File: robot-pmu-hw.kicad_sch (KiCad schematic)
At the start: 0 parts

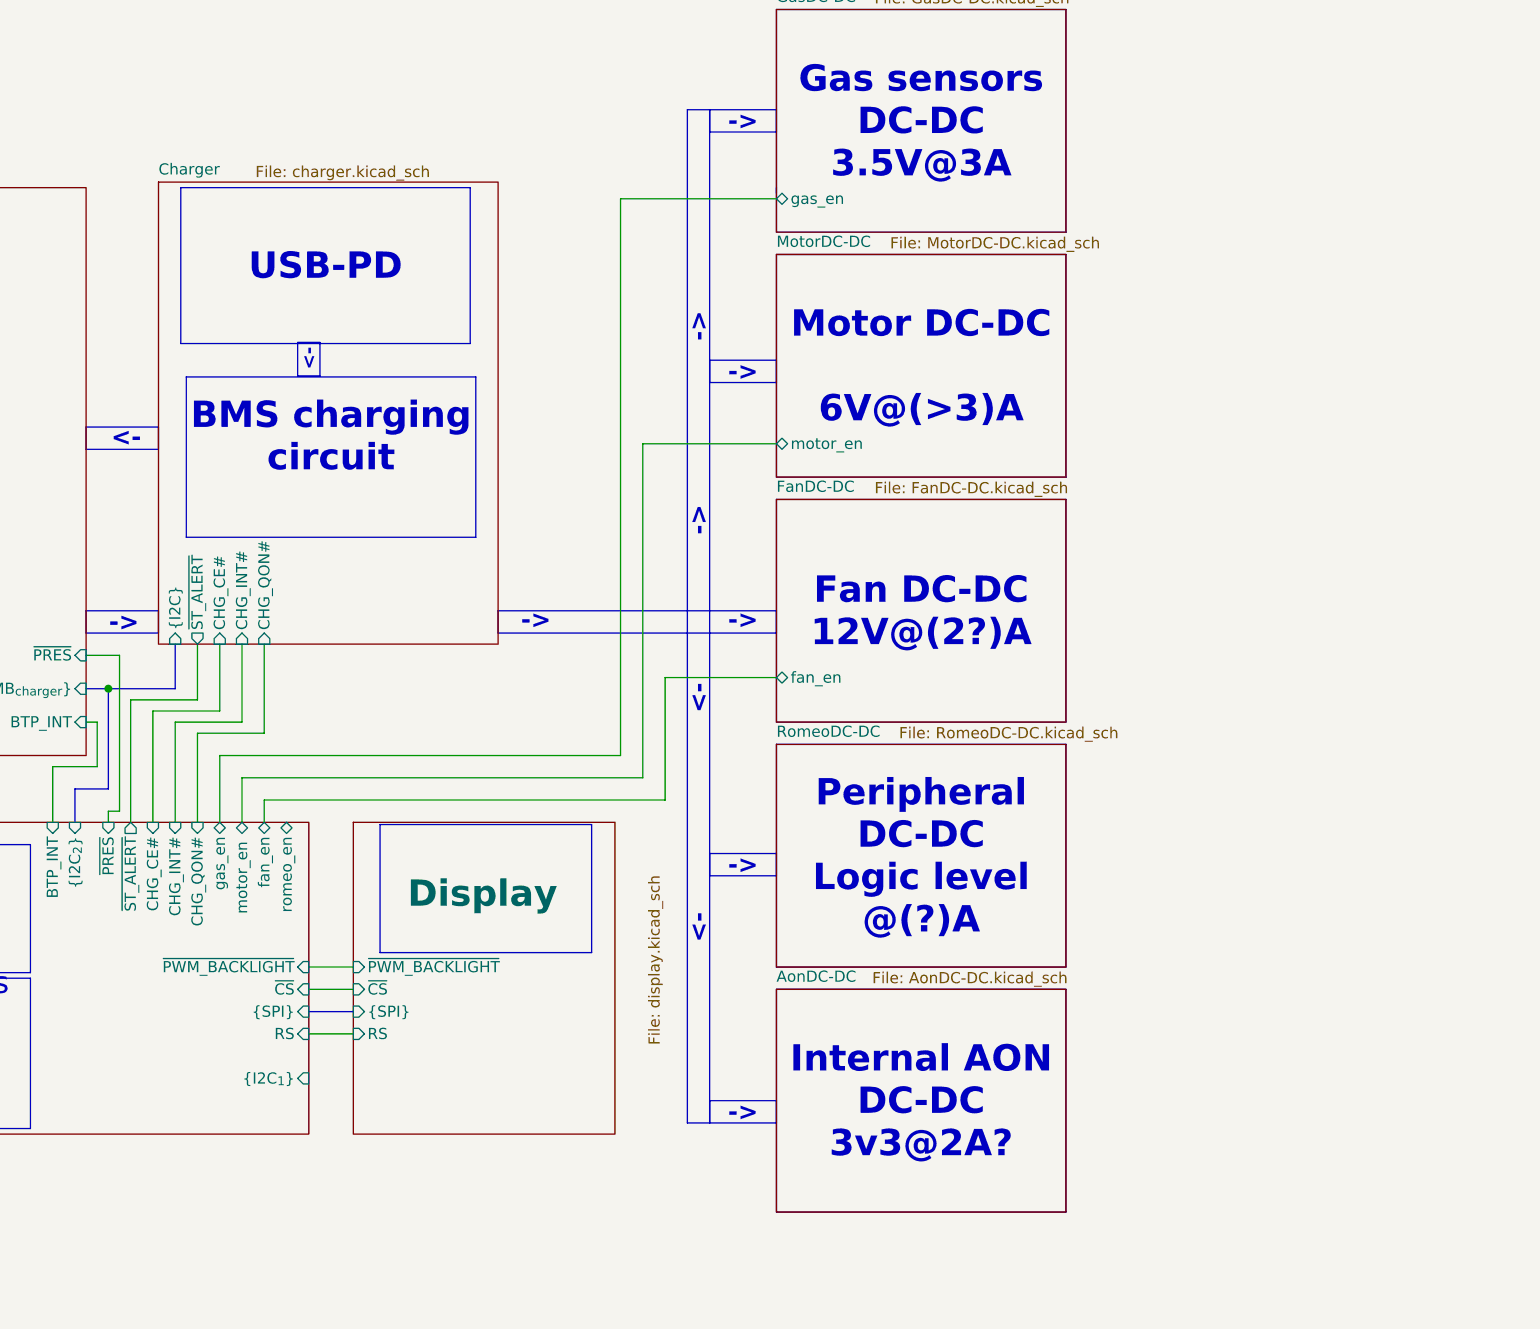
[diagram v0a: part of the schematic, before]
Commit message: Minimal version without BMS
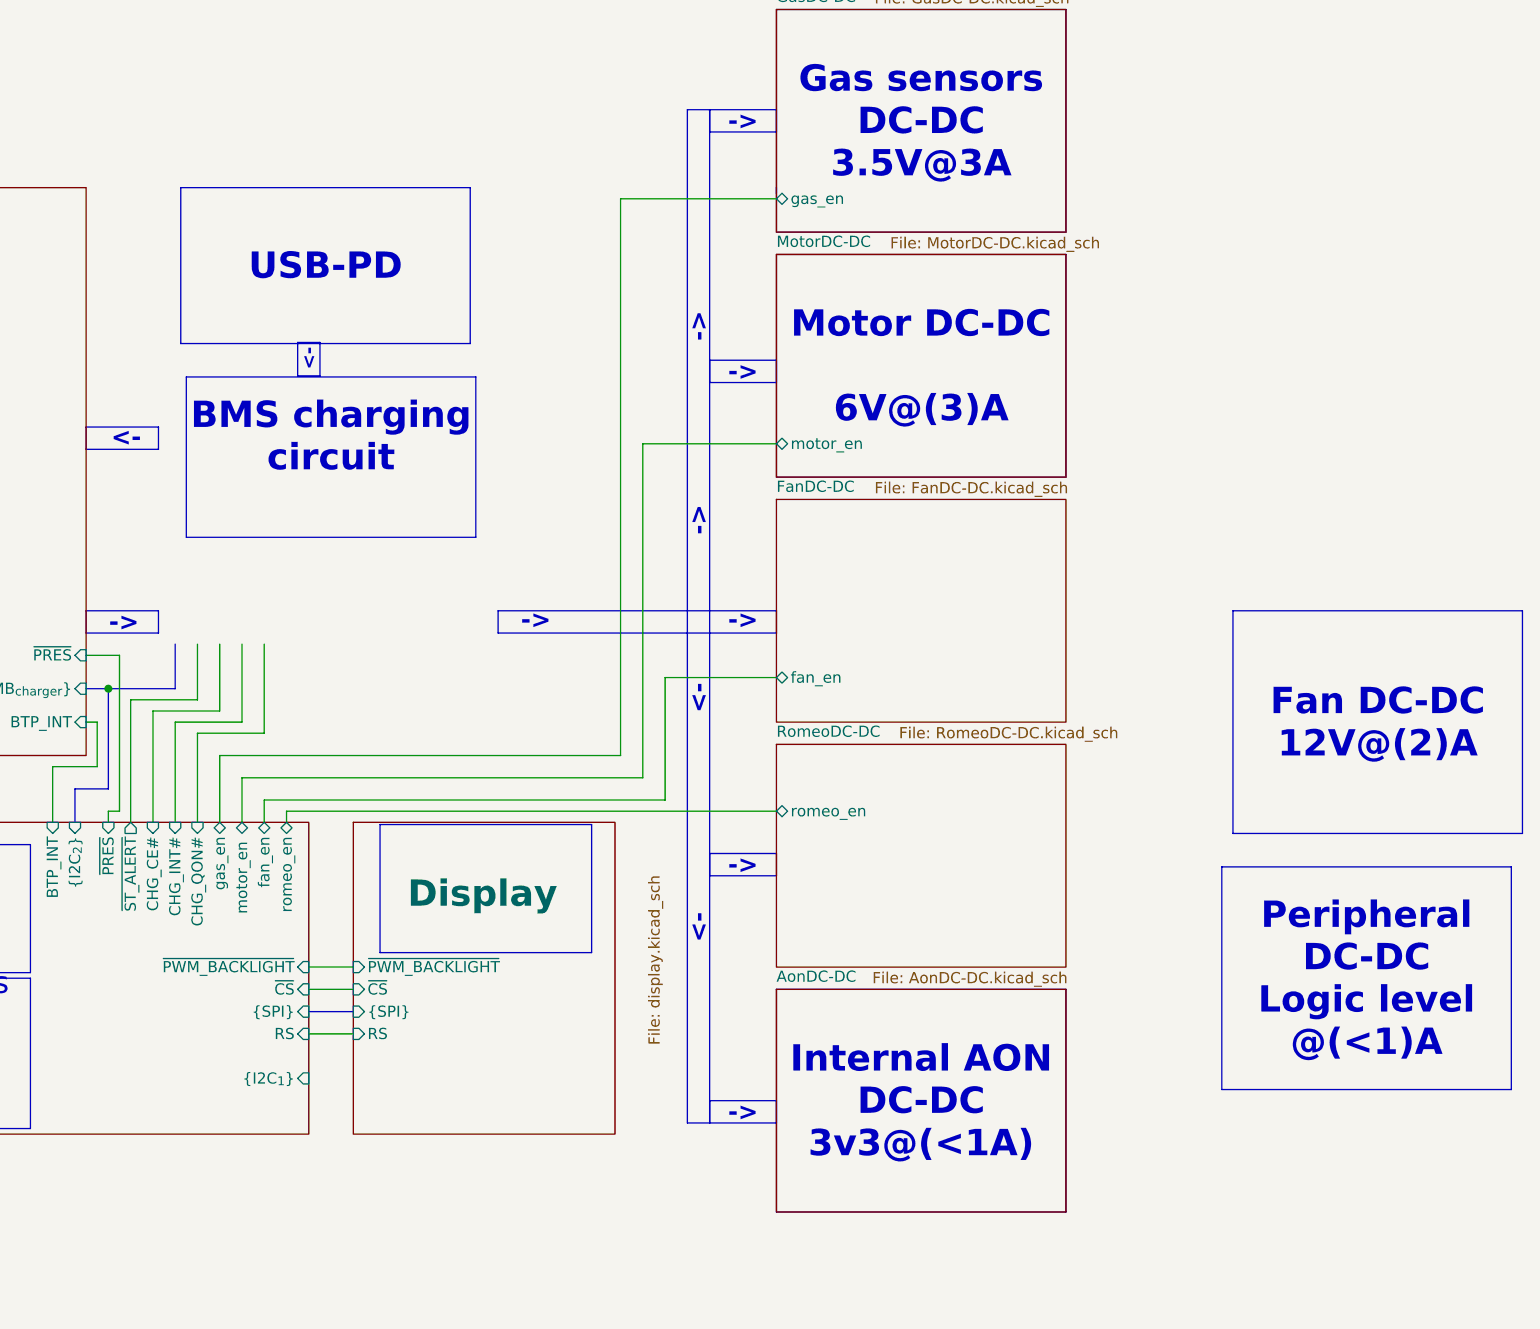
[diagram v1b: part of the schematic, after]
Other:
- removed sheet Charger
- sheet RomeoDC-DC ports: added romeo_en; removed none
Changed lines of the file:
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@@
 		)
 	)
-	(text_box "Internal AON DC-DC \n3v3@2A?"
+	(text_box "Internal AON DC-DC \n3v3@(<1A)"
 		(exclude_from_sim no)
 		(at 267.97 179.07 0)
@@
 		)
 	)
-	(text_box "Fan DC-DC \n12V@(2?)A"
-		(exclude_from_sim no)
-		(at 267.97 123.19 0)
+	(text_box "Fan DC-DC \n12V@(2)A"
+		(exclude_from_sim no)
+		(at 320.04 135.89 0)
 		(size 33.02 25.4)
 		(margins 0.9525 0.9525 0.9525 0.9525)
@@
 		)
 	)
-	(text_box "Motor DC-DC \n6V@(>3)A"
+	(text_box "Motor DC-DC \n6V@(3)A"
 		(exclude_from_sim no)
 		(at 267.97 95.25 0)
@@
 		)
 	)
-	(text_box "Peripheral DC-DC \nLogic level @(?)A"
-		(exclude_from_sim no)
-		(at 267.97 151.13 0)
+	(text_box "Peripheral DC-DC \nLogic level @(<1)A"
+		(exclude_from_sim no)
+		(at 318.77 165.1 0)
 		(size 33.02 25.4)
 		(margins 0.9525 0.9525 0.9525 0.9525)
@@
 	(wire
 		(pts
+			(xy 212.09 160.02) (xy 212.09 158.75)
+		)
+		(stroke
+			(width 0)
+			(type default)
+		)
+	)
+	(wire
+		(pts
 			(xy 252.73 154.94) (xy 252.73 116.84)
 		)
@@
 			(type default)
 			(color 227 93 255 1)
+		)
+	)
+	(wire
+		(pts
+			(xy 212.09 158.75) (xy 267.97 158.75)
+		)
+		(stroke
+			(width 0)
+			(type default)
 		)
 	)
@@
 			)
 		)
+		(pin "romeo_en" bidirectional
+			(at 267.97 158.75 180)
+			(effects
+				(font
+					(size 1.27 1.27)
+				)
+				(justify left)
+			)
+		)
 		(instances
 			(project "robot-pmu-hw"
@@
 				)
 			)
-		)
-	)
-	(sheet
-		(at 197.485 86.995)
-		(size 38.735 52.705)
-		(exclude_from_sim no)
-		(in_bom yes)
-		(on_board yes)
-		(dnp no)
-		(stroke
-			(width 0.1524)
-			(type solid)
-		)
-		(fill
-			(color 130 179 102 1.0000)
-		)
-		(property "Sheetname" "Charger"
-			(at 197.485 86.2834 0)
-			(effects
-				(font
-					(size 1.27 1.27)
-				)
-				(justify left bottom)
-			)
-		)
-		(property "Sheetfile" "charger.kicad_sch"
-			(at 208.534 85.09 0)
-			(effects
-				(font
-					(size 1.27 1.27)
-				)
-				(justify left top)
-			)
-		)
-		(pin "~{ST_ALERT}" output
-			(at 201.93 139.7 270)
-			(effects
-				(font
-					(size 1.27 1.27)
-				)
-				(justify left)
-			)
-		)
-		(pin "CHG_CE#" input
-			(at 204.47 139.7 270)
-			(effects
-				(font
-					(size 1.27 1.27)
-				)
-				(justify left)
-			)
-		)
-		(pin "CHG_INT#" input
-			(at 207.01 139.7 270)
-			(effects
-				(font
-					(size 1.27 1.27)
-				)
-				(justify left)
-			)
-		)
-		(pin "CHG_QON#" input
-			(at 209.55 139.7 270)
-			(effects
-				(font
-					(size 1.27 1.27)
-				)
-				(justify left)
-			)
-		)
-		(pin "{I2C}" input
-			(at 199.39 139.7 270)
-			(effects
-				(font
-					(size 1.27 1.27)
-				)
-				(justify left)
-			)
-		)
-		(instances
-			(project "robot-pmu-hw"
-				(path "/ca7f4c4c-3c96-472a-b66f-ec124f8cf9b5"
-					(page "10")
-				)
-			)
